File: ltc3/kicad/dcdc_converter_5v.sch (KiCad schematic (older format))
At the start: 0 parts

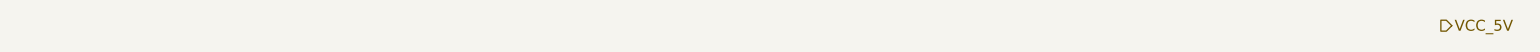
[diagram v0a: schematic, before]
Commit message: More work on LTC3 schematic. 1. Created placeholder "power in" schematic. 2. First cut at external trigger schematic (MOSTFETs and mechanical    relays).
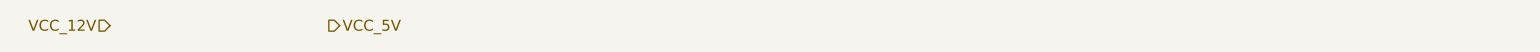
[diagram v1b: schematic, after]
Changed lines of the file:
@@
 LIBS:LTC299x
 LIBS:memory_devices
+LIBS:switches
 LIBS:Launch_Tower_Computer_III-cache
 EELAYER 27 0
@@
 $Descr USLetter 11000 8500
 encoding utf-8
-Sheet 3 4
+Sheet 3 6
 Title "LTC3 12V-to-5V DC/DC Converter"
-Date "16 mar 2015"
+Date "2 apr 2015"
 Rev "1"
 Comp "Portland State Aerospace Society <http://psas.pdx.edu/>"
@@
 Comment4 ""
 $EndDescr
-Text HLabel 9050 1900 2    60   Output ~ 0
+Text HLabel 2950 1900 2    60   Output ~ 0
 VCC_5V
+Text HLabel 1750 1900 0    60   Input ~ 0
+VCC_12V
 $EndSCHEMATC

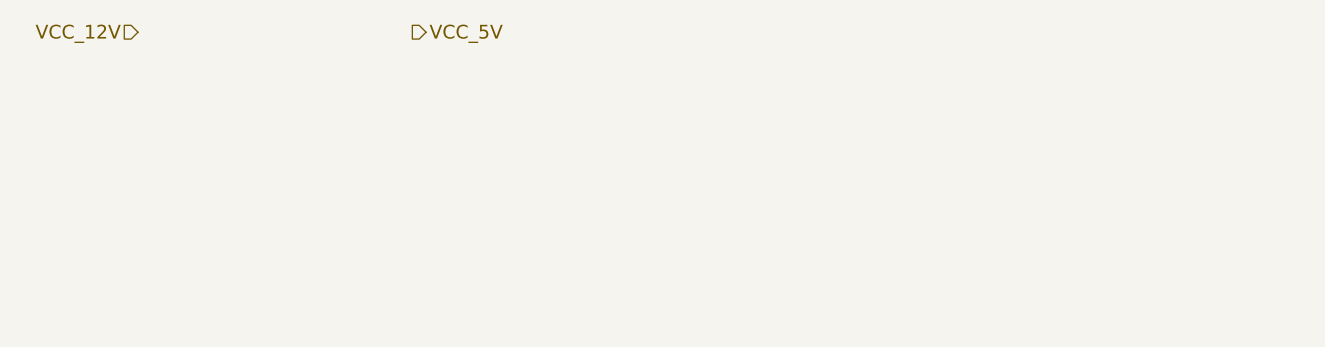
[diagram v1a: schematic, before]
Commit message: Fixed mistakes in triggers schematic; misc. clean-up.
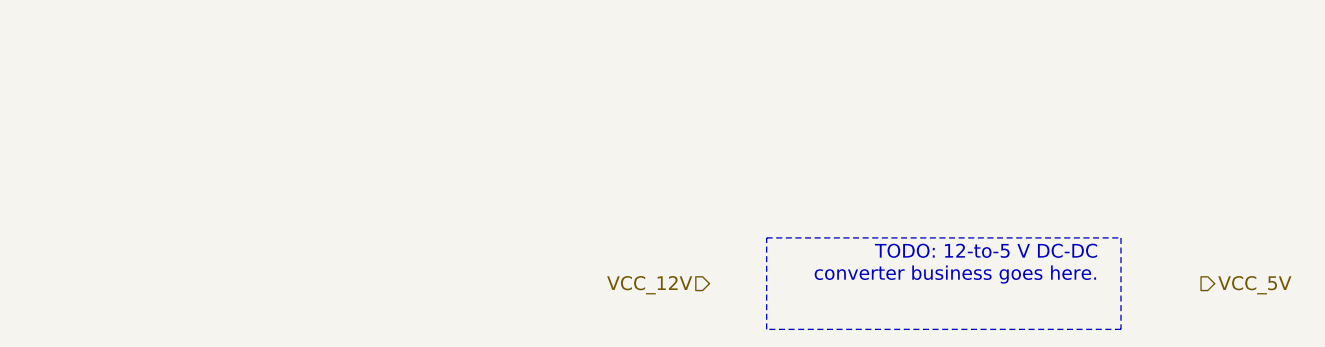
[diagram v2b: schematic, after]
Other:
- note added: "TODO: 12-to-5 V DC-DC\nconverter business goes here."
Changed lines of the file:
@@
 Comment4 ""
 $EndDescr
-Text HLabel 2950 1900 2    60   Output ~ 0
+Text HLabel 6400 3000 2    60   Output ~ 0
 VCC_5V
-Text HLabel 1750 1900 0    60   Input ~ 0
+Text HLabel 4250 3000 0    60   Input ~ 0
 VCC_12V
+Text Notes 5950 3000 2    60   ~ 0
+TODO: 12-to-5 V DC-DC\nconverter business goes here.
+Wire Notes Line
+	4500 2800 6050 2800
+Wire Notes Line
+	6050 2800 6050 3200
+Wire Notes Line
+	6050 3200 4500 3200
+Wire Notes Line
+	4500 3200 4500 2800
 $EndSCHEMATC

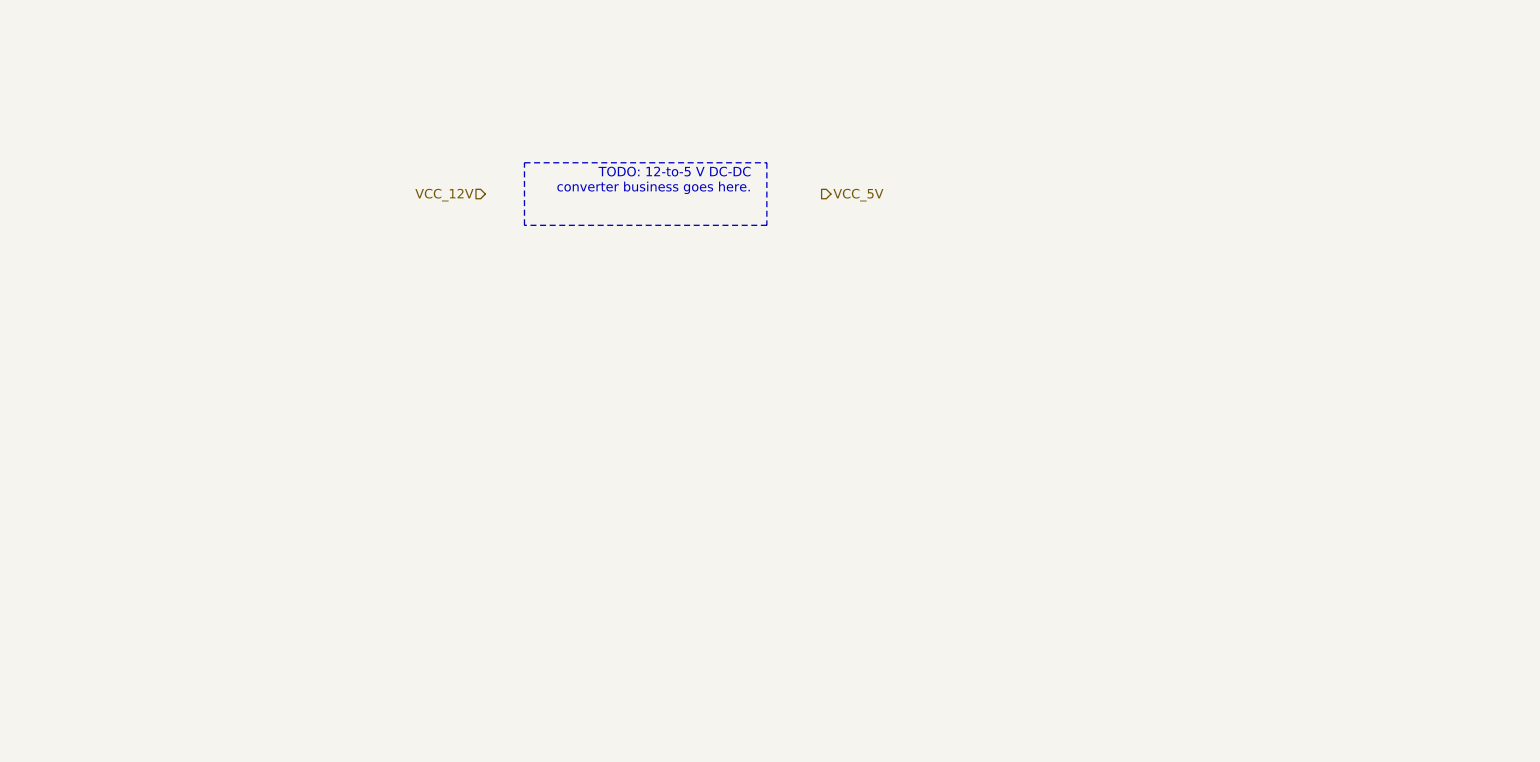
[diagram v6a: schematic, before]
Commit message: LTC3 KiCad updates. 1. Modified schematics to play nicely with (relatively) recent changes    in KiCad's stock component libraries (e.g., redrawn capacitor and    resistor symbols). 2. Began work on PTN78020-based DC-DC converter schematics.
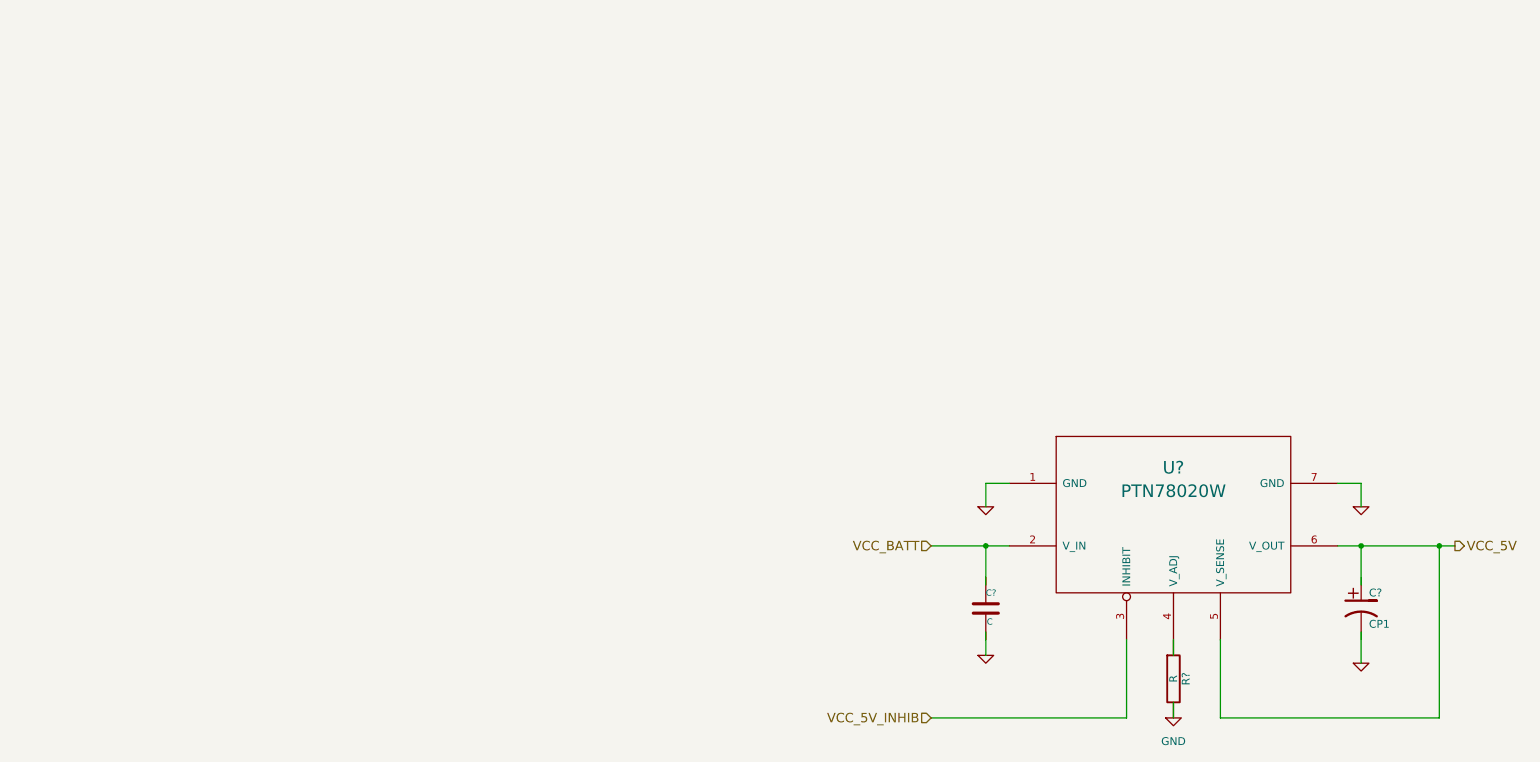
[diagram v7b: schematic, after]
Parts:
- added C?: CP1, ~, symbol CP1
- added C?: C, ~, symbol C
- added R?: R, symbol R
- added U?: PTN78020W, ~, symbol PTN78020W
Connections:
- net labels added: GND, VCC_5V_INHIB, VCC_BATT
- net labels removed: VCC_12V
- wire segments 0 -> 17
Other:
- note removed: "TODO: 12-to-5 V DC-DC\nconverter business goes here."
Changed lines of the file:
@@
 LIBS:memory
 LIBS:xilinx
-LIBS:special
 LIBS:microcontrollers
 LIBS:dsp
@@
 LIBS:switches
 LIBS:Toshiba
+LIBS:LTC3_components
 LIBS:Launch_Tower_Computer_III-cache
-EELAYER 27 0
+EELAYER 25 0
 EELAYER END
 $Descr B 17000 11000
@@
 Sheet 3 7
 Title "LTC3 12V-to-5V DC/DC Converter"
-Date "18 apr 2015"
+Date "16 may 2015"
 Rev "1"
 Comp "Portland State Aerospace Society <http://psas.pdx.edu/>"
@@
 Comment4 ""
 $EndDescr
-Text HLabel 6400 3000 2    60   Output ~ 0
+Text HLabel 10450 5250 2    60   Output ~ 0
 VCC_5V
-Text HLabel 4250 3000 0    60   Input ~ 0
-VCC_12V
-Text Notes 5950 3000 2    60   ~ 0
-TODO: 12-to-5 V DC-DC\nconverter business goes here.
-Wire Notes Line
-	4500 2800 6050 2800
-Wire Notes Line
-	6050 2800 6050 3200
-Wire Notes Line
-	6050 3200 4500 3200
-Wire Notes Line
-	4500 3200 4500 2800
+Text HLabel 7100 5250 0    60   Input ~ 0
+VCC_BATT
+$Comp
+L PTN78020W U?
+U 1 1 5557F694
+P 8650 5050
+F 0 "U?" H 8650 5350 80  0000 C CNN
+F 1 "PTN78020W" H 8650 5200 80  0000 C CNN
+F 2 "~" H 8650 5100 60  0000 C CNN
+F 3 "~" H 8650 5100 60  0000 C CNN
+	1    8650 5050
+	1    0    0    -1
+$EndComp
+$Comp
+L GND #PWR?
+U 1 1 5557F6A3
+P 7450 5000
+AR Path="/5557F6A3" Ref="#PWR?"  Part="1"
+AR Path="/550535FB/5557F6A3" Ref="#PWR?"  Part="1"
+F 0 "#PWR?" H 7450 5000 30  0001 C CNN
+F 1 "GND" H 7450 4930 30  0001 C CNN
+F 2 "" H 7450 5000 60  0000 C CNN
+F 3 "" H 7450 5000 60  0000 C CNN
+	1    7450 5000
+	1    0    0    -1
+$EndComp
+$Comp
+L GND #PWR?
+U 1 1 5557F6B2
+P 9850 5000
+AR Path="/5557F6B2" Ref="#PWR?"  Part="1"
+AR Path="/550535FB/5557F6B2" Ref="#PWR?"  Part="1"
+F 0 "#PWR?" H 9850 5000 30  0001 C CNN
+F 1 "GND" H 9850 4930 30  0001 C CNN
+F 2 "" H 9850 5000 60  0000 C CNN
+F 3 "" H 9850 5000 60  0000 C CNN
+	1    9850 5000
+	1    0    0    -1
+$EndComp
+Wire Wire Line
+	7600 4850 7450 4850
+Wire Wire Line
+	7450 4850 7450 5000
+Wire Wire Line
+	9700 4850 9850 4850
+Wire Wire Line
+	9850 4850 9850 5000
+Wire Wire Line
+	9700 5250 10450 5250
+Wire Wire Line
+	7100 5250 7600 5250
+$Comp
+L CP1 C?
+U 1 1 5557F6DE
+P 9850 5650
+AR Path="/5557F6DE" Ref="C?"  Part="1"
+AR Path="/550535FB/5557F6DE" Ref="C?"  Part="1"
+F 0 "C?" H 9900 5750 50  0000 L CNN
+F 1 "CP1" H 9900 5550 50  0000 L CNN
+F 2 "~" H 9850 5650 60  0000 C CNN
+F 3 "~" H 9850 5650 60  0000 C CNN
+	1    9850 5650
+	1    0    0    -1
+$EndComp
+$Comp
+L GND #PWR?
+U 1 1 5557F6ED
+P 9850 6000
+AR Path="/5557F6ED" Ref="#PWR?"  Part="1"
+AR Path="/550535FB/5557F6ED" Ref="#PWR?"  Part="1"
+F 0 "#PWR?" H 9850 6000 30  0001 C CNN
+F 1 "GND" H 9850 5930 30  0001 C CNN
+F 2 "" H 9850 6000 60  0000 C CNN
+F 3 "" H 9850 6000 60  0000 C CNN
+	1    9850 6000
+	1    0    0    -1
+$EndComp
+Wire Wire Line
+	9850 5500 9850 5250
+Connection ~ 9850 5250
+Wire Wire Line
+	9850 5800 9850 6000
+$Comp
+L C C?
+U 1 1 5557F70C
+P 7450 5650
+AR Path="/5557F70C" Ref="C?"  Part="1"
+AR Path="/550535FB/5557F70C" Ref="C?"  Part="1"
+F 0 "C?" H 7450 5750 40  0000 L CNN
+F 1 "C" H 7456 5565 40  0000 L CNN
+F 2 "~" H 7488 5500 30  0000 C CNN
+F 3 "~" H 7450 5650 60  0000 C CNN
+	1    7450 5650
+	1    0    0    -1
+$EndComp
+$Comp
+L GND #PWR?
+U 1 1 5557F71B
+P 7450 5950
+AR Path="/5557F71B" Ref="#PWR?"  Part="1"
+AR Path="/550535FB/5557F71B" Ref="#PWR?"  Part="1"
+F 0 "#PWR?" H 7450 5950 30  0001 C CNN
+F 1 "GND" H 7450 5880 30  0001 C CNN
+F 2 "" H 7450 5950 60  0000 C CNN
+F 3 "" H 7450 5950 60  0000 C CNN
+	1    7450 5950
+	1    0    0    -1
+$EndComp
+Wire Wire Line
+	7450 5950 7450 5800
+Wire Wire Line
+	7450 5500 7450 5250
+Connection ~ 7450 5250
+$Comp
+L R R?
+U 1 1 555D0B08
+P 8650 6100
+F 0 "R?" V 8730 6100 50  0000 C CNN
+F 1 "R" V 8650 6100 50  0000 C CNN
+F 2 "" V 8580 6100 30  0000 C CNN
+F 3 "" H 8650 6100 30  0000 C CNN
+	1    8650 6100
+	1    0    0    -1
+$EndComp
+$Comp
+L GND #PWR?
+U 1 1 555D0B2F
+P 8650 6350
+F 0 "#PWR?" H 8650 6100 50  0001 C CNN
+F 1 "GND" H 8650 6200 50  0000 C CNN
+F 2 "" H 8650 6350 60  0000 C CNN
+F 3 "" H 8650 6350 60  0000 C CNN
+	1    8650 6350
+	1    0    0    -1
+$EndComp
+Wire Wire Line
+	8650 6350 8650 6250
+Wire Wire Line
+	8650 5950 8650 5850
+Text HLabel 7100 6350 0    60   Input ~ 0
+VCC_5V_INHIB
+Wire Wire Line
+	8350 5850 8350 6350
+Wire Wire Line
+	8350 6350 7100 6350
+Wire Wire Line
+	8950 5850 8950 6350
+Wire Wire Line
+	8950 6350 10350 6350
+Wire Wire Line
+	10350 6350 10350 5250
+Connection ~ 10350 5250
 $EndSCHEMATC
